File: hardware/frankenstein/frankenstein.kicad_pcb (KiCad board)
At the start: 2 copper layers, 100 x 99.9 mm, 261 parts, among them J351 MINI-USB-5P-3400020P1, M200 CONN_1, M201 CONN_1, M202 CONN_1, M351 CONN_1, M352 CONN_1, M401 CONN_1, M470 CONN_1, M471 CONN_1, P104 CONN_4, P201 CONN_10X2, P202 CONN_3, P203 CONN_2, P204 CONN_1, P205 CONN_1, P208 CONN_6, P209 CONN_6, P351 CONN_5X2, P352 MICRO-SDCARD-CONNECTOR-330006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, P353 CONN_10X2, P356 CONN_1, P401 CONN_3, P402 CONN_10X2, P403 CONN_16, P404 CONN_1, P405 CONN_1, P472 CONN_2, P51 CONN_4X2, P52 CONN_10X2, P53 CONN_2, P54 CONN_5X2, P55 CONN_6, P56 CONN_6, P57 CONN_6, P58 CONN_6, P603 CONN_6, P610 CONN_1, Q401 OVP_DRIVER, Q402 OVP_DRIVER, Q403 OVP_DRIVER, Q404 OVP_DRIVER, Q405 OVP_DRIVER, Q406 OVP_DRIVER, Q407 OVP_DRIVER, Q408 OVP_DRIVER, Q409 OVP_DRIVER, Q410 OVP_DRIVER, Q411 OVP_DRIVER, Q412 OVP_DRIVER, U101 MAX9926/9927, U201 LMV324IDR, U202 LMV324IDR, U203 LMV324IDR, U351 FT232RL, U471 SN65HVD230, U601 TC4427AVOA, U602 TC4427AVOA, U603 TC4427AVOA

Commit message: RC2
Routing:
- net GND: track 636.1 -> 611.2 mm, vias 267 -> 264
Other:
- net class Default: clearance 0.2032 -> 0.1778
- rule trace_clearance: 0.2032 -> 0.1778
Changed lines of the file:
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@@
   (general
     (links 592)
-    (no_connects 1)
+    (no_connects 0)
     (area 96.266 79.121 266.827001 205.740001)
     (thickness 1.6)
     (drawings 371)
-    (tracks 3153)
+    (tracks 3134)
     (zones 0)
     (modules 261)
@@
     (19 F.Paste user)
     (20 B.SilkS user)
-    (21 F.SilkS user)
+    (21 F.SilkS user hide)
     (22 B.Mask user)
     (23 F.Mask user)
@@
   (setup
     (last_trace_width 0.254)
-    (trace_clearance 0.2032)
+    (trace_clearance 0.1778)
     (zone_clearance 0.254)
     (zone_45_only no)
@@
     (pad_to_mask_clearance 0)
     (aux_axis_origin 0 0)
-    (visible_elements 7FFFFFBF)
+    (visible_elements 7FFFFFAF)
     (pcbplotparams
       (layerselection 318537729)
@@
   (net 185 GND)
   (net_class Default "This is the default net class."
-    (clearance 0.2032)
+    (clearance 0.1778)
     (trace_width 0.254)
     (via_dia 0.889)
@@
   (segment (start 164.465 126.365) (end 163.195 126.365) (width 0.254) (layer F.Cu) (net 70))
   (segment (start 127 149.819) (end 127 149.8194) (width 0.254) (layer F.Cu) (net 70))
+  (segment (start 127 142.19936) (end 126.95936 142.19936) (width 0.254) (layer F.Cu) (net 71))
+  (segment (start 121.919798 118.427702) (end 123.5075 116.84) (width 0.254) (layer F.Cu) (net 71))
+  (segment (start 121.919798 137.159798) (end 121.919798 118.427702) (width 0.254) (layer F.Cu) (net 71))
+  (segment (start 126.95936 142.19936) (end 121.919798 137.159798) (width 0.254) (layer F.Cu) (net 71))
   (segment (start 123.508 114.3) (end 123.508 115.57) (width 0.254) (layer F.Cu) (net 71))
   (segment (start 123.508 116.84) (end 123.5075 116.84) (width 0.254) (layer F.Cu) (net 71))
@@
   (segment (start 123.5075 115.5695) (end 123.5075 114.3) (width 0.254) (layer F.Cu) (net 71))
   (segment (start 123.508 115.57) (end 123.5075 115.5695) (width 0.254) (layer F.Cu) (net 71))
-  (segment (start 127 142.199) (end 127 142.1994) (width 0.254) (layer F.Cu) (net 71))
-  (segment (start 121.92 137.119) (end 127 142.199) (width 0.254) (layer F.Cu) (net 71))
-  (segment (start 121.92 118.11) (end 121.92 137.119) (width 0.254) (layer F.Cu) (net 71))
-  (segment (start 123.19 116.84) (end 121.92 118.11) (width 0.254) (layer F.Cu) (net 71))
-  (segment (start 123.5075 116.84) (end 123.19 116.84) (width 0.254) (layer F.Cu) (net 71))
   (segment (start 139.382 116.84) (end 139.382 115.57) (width 0.254) (layer F.Cu) (net 72))
   (segment (start 139.3825 116.84) (end 139.382 116.84) (width 0.254) (layer F.Cu) (net 72))
@@
   (segment (start 209.804 159.385) (end 210.439 160.02) (width 0.254) (layer F.Cu) (net 137))
   (segment (start 204.1525 159.385) (end 209.804 159.385) (width 0.254) (layer F.Cu) (net 137))
-  (segment (start 204.152 156.845) (end 204.1525 156.845) (width 0.254) (layer F.Cu) (net 138))
-  (segment (start 209.22 157.429) (end 210.439 156.21) (width 0.254) (layer F.Cu) (net 138))
-  (segment (start 205.105 157.429) (end 209.22 157.429) (width 0.254) (layer F.Cu) (net 138))
-  (segment (start 204.521 156.845) (end 205.105 157.429) (width 0.254) (layer F.Cu) (net 138))
-  (segment (start 204.1525 156.845) (end 204.521 156.845) (width 0.254) (layer F.Cu) (net 138))
+  (segment (start 204.1525 156.845) (end 204.597402 156.845) (width 0.254) (layer F.Cu) (net 138))
+  (segment (start 209.194802 157.454198) (end 210.439 156.21) (width 0.254) (layer F.Cu) (net 138))
+  (segment (start 205.2066 157.454198) (end 209.194802 157.454198) (width 0.254) (layer F.Cu) (net 138))
+  (segment (start 204.597402 156.845) (end 205.2066 157.454198) (width 0.254) (layer F.Cu) (net 138))
   (segment (start 164.38 186.826) (end 164.38 186.8255) (width 0.254) (layer F.Cu) (net 139))
   (segment (start 164.38 186.8255) (end 164.38 185.302) (width 0.254) (layer F.Cu) (net 139))
@@
   (segment (start 134.239 114.3) (end 137.4775 114.3) (width 0.254) (layer F.Cu) (net 184))
   (segment (start 137.4775 114.3) (end 137.478 114.3) (width 0.254) (layer F.Cu) (net 184))
+  (segment (start 198.438 174.7345) (end 196.7055 174.7345) (width 0.254) (layer F.Cu) (net 185))
+  (via (at 196.596 174.625) (size 0.889) (layers F.Cu B.Cu) (net 185))
+  (segment (start 196.7055 174.7345) (end 196.596 174.625) (width 0.254) (layer F.Cu) (net 185))
   (via (at 159.205 176.126) (size 0.889) (layers F.Cu B.Cu) (net 185))
   (via (at 156.03 176.126) (size 0.889) (layers F.Cu B.Cu) (net 185))
@@
   (via (at 151.448 119.062) (size 0.889) (layers F.Cu B.Cu) (net 185))
   (via (at 172.402 119.062) (size 0.889) (layers F.Cu B.Cu) (net 185))
-  (via (at 189.674 172.956) (size 0.889) (layers F.Cu B.Cu) (net 185))
   (via (at 183.896 189.53) (size 0.889) (layers F.Cu B.Cu) (net 185))
   (via (at 197.104 189.53) (size 0.889) (layers F.Cu B.Cu) (net 185))
@@
   (via (at 195.834 186.228) (size 0.889) (layers F.Cu B.Cu) (net 185))
   (via (at 199.136 184.704) (size 0.889) (layers F.Cu B.Cu) (net 185))
-  (via (at 184.15 166.797) (size 0.889) (layers F.Cu B.Cu) (net 185))
-  (via (at 184.023 168.702) (size 0.889) (layers F.Cu B.Cu) (net 185))
-  (via (at 193.421 172.956) (size 0.889) (layers F.Cu B.Cu) (net 185))
   (via (at 204.343 175.306) (size 0.889) (layers F.Cu B.Cu) (net 185))
   (via (at 209.55 175.306) (size 0.889) (layers F.Cu B.Cu) (net 185))
@@
   (segment (start 200.787 184.704) (end 200.914 184.577) (width 0.254) (layer F.Cu) (net 185))
   (segment (start 199.136 184.704) (end 200.787 184.704) (width 0.254) (layer F.Cu) (net 185))
-  (segment (start 188.087 166.67) (end 190.627 167.432) (width 0.254) (layer F.Cu) (net 185))
-  (segment (start 184.277 166.67) (end 188.087 166.67) (width 0.254) (layer F.Cu) (net 185))
-  (segment (start 184.15 166.797) (end 184.277 166.67) (width 0.254) (layer F.Cu) (net 185))
-  (segment (start 184.15 168.575) (end 184.15 166.797) (width 0.254) (layer B.Cu) (net 185))
-  (segment (start 184.023 168.702) (end 184.15 168.575) (width 0.254) (layer B.Cu) (net 185))
-  (segment (start 184.531 169.21) (end 184.023 168.702) (width 0.254) (layer F.Cu) (net 185))
-  (segment (start 184.531 170.988) (end 184.531 169.21) (width 0.254) (layer F.Cu) (net 185))
-  (segment (start 185.801 172.258) (end 184.531 170.988) (width 0.254) (layer F.Cu) (net 185))
-  (segment (start 188.976 172.258) (end 185.801 172.258) (width 0.254) (layer F.Cu) (net 185))
-  (segment (start 189.674 172.956) (end 188.976 172.258) (width 0.254) (layer F.Cu) (net 185))
-  (segment (start 189.674 172.956) (end 193.421 172.956) (width 0.254) (layer B.Cu) (net 185))
-  (segment (start 196.947 174.734) (end 198.438 174.734) (width 0.254) (layer F.Cu) (net 185))
-  (segment (start 196.629 175.052) (end 196.947 174.734) (width 0.254) (layer F.Cu) (net 185))
-  (segment (start 195.105 173.528) (end 196.629 175.052) (width 0.254) (layer F.Cu) (net 185))
-  (segment (start 193.992 173.528) (end 195.105 173.528) (width 0.254) (layer F.Cu) (net 185))
-  (segment (start 193.421 172.956) (end 193.992 173.528) (width 0.254) (layer F.Cu) (net 185))
   (segment (start 204.343 175.306) (end 209.55 175.306) (width 0.254) (layer B.Cu) (net 185))
   (segment (start 204.343 174.29) (end 204.343 175.306) (width 0.254) (layer F.Cu) (net 185))

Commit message: RC2
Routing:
- net /3.3V: track 215.7 -> 192.5 mm, vias 1 -> 2
- net GND: track 611.2 -> 607.9 mm

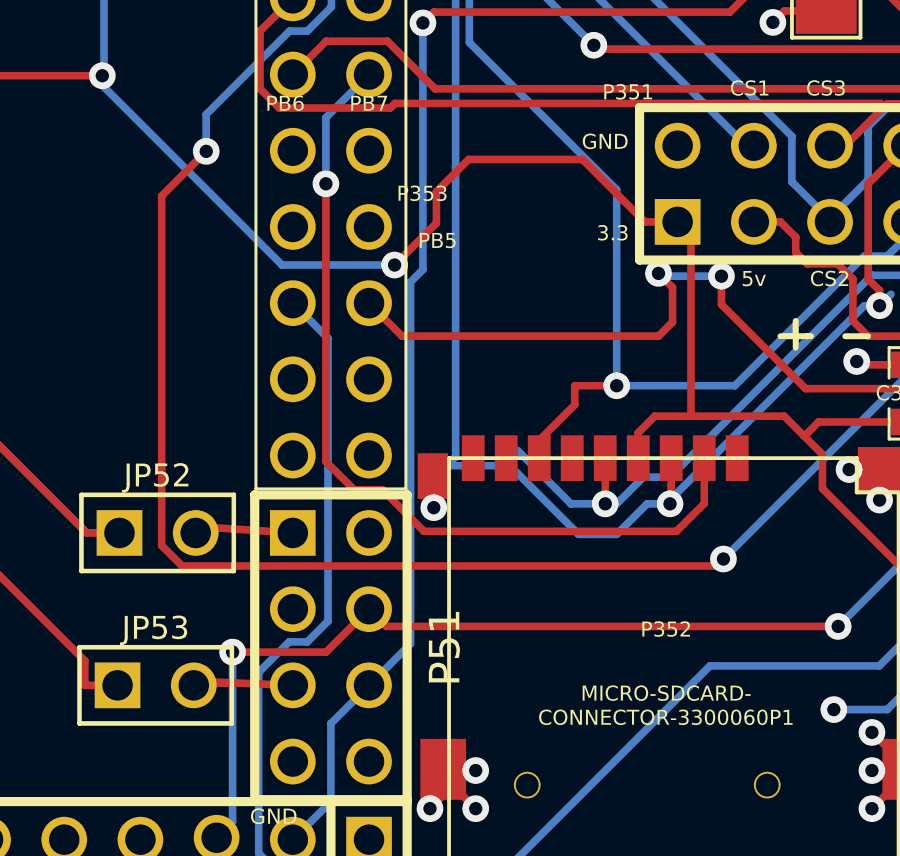
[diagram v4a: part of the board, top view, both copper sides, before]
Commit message: RX/TX flip
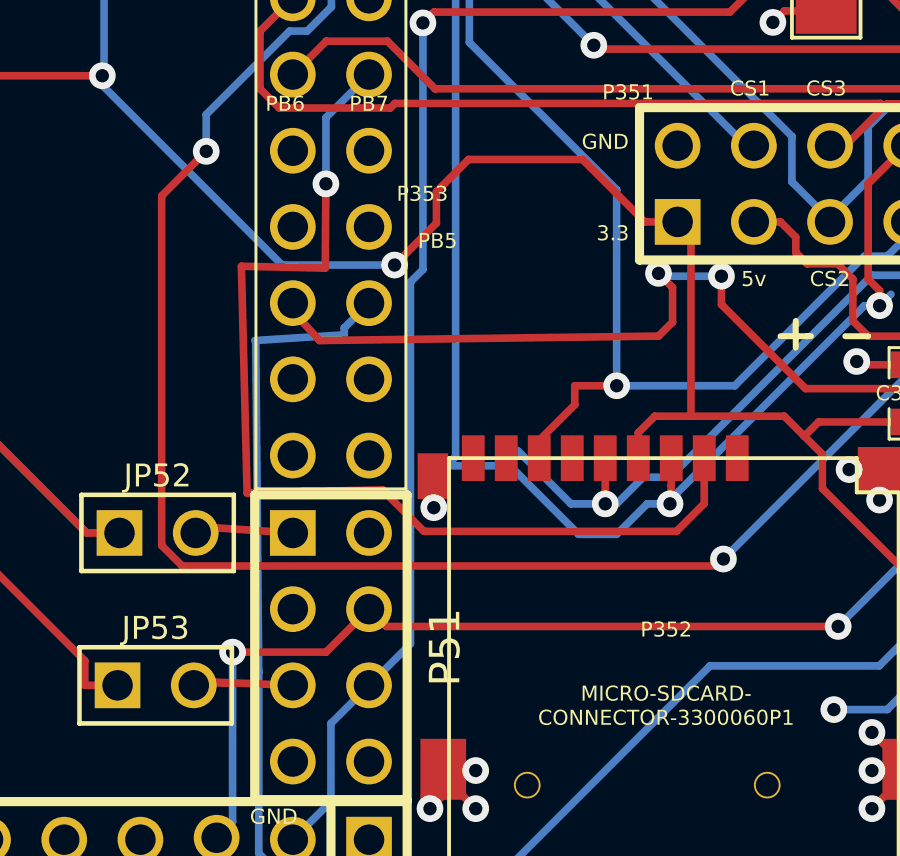
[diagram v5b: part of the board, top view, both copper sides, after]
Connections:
- P353 pad 15: /USART_TX -> /USART_RX
- P353 pad 16: /USART_RX -> /USART_TX
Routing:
- net /CS_SD_MODULE: track 29.0 -> 35.1 mm
- net /USART_RX: track 34.4 -> 37.1 mm
- net /USART_TX: track 88.1 -> 89.4 mm
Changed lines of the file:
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@@
     (thickness 1.6)
     (drawings 371)
-    (tracks 3119)
+    (tracks 3120)
     (zones 0)
     (modules 261)
@@
     (pad_to_mask_clearance 0)
     (aux_axis_origin 0 0)
-    (visible_elements 7FFFFF3F)
+    (visible_elements 7FFF9F3F)
     (pcbplotparams
       (layerselection 318537729)
@@
     (pad 15 thru_hole circle (at 6.30936 1.27 270) (size 1.524 1.524) (drill 1.016)
       (layers *.Cu *.Mask F.SilkS)
-      (net 103 /USART_TX)
+      (net 102 /USART_RX)
     )
     (pad 16 thru_hole circle (at 6.30936 -1.27 270) (size 1.524 1.524) (drill 1.016)
       (layers *.Cu *.Mask F.SilkS)
-      (net 102 /USART_RX)
+      (net 103 /USART_TX)
     )
     (pad 17 thru_hole circle (at 8.84936 1.27 270) (size 1.524 1.524) (drill 1.016)
@@
   (segment (start 200.787 167.432) (end 202.8817 169.5267) (width 0.254) (layer F.Cu) (net 16))
   (via (at 178.9026 168.702) (size 0.889) (layers F.Cu B.Cu) (net 17))
-  (segment (start 178.9026 177.9601) (end 178.9026 168.702) (width 0.254) (layer F.Cu) (net 17))
-  (segment (start 179.8451 178.9026) (end 178.9026 177.9601) (width 0.254) (layer F.Cu) (net 17))
-  (segment (start 180.7877 178.9026) (end 179.8451 178.9026) (width 0.254) (layer F.Cu) (net 17))
+  (segment (start 176.0855 171.45) (end 178.8795 171.5135) (width 0.254) (layer F.Cu) (net 17))
+  (segment (start 178.8795 171.5135) (end 178.9026 168.702) (width 0.254) (layer F.Cu) (net 17))
+  (segment (start 176.276 179.0065) (end 176.0855 171.45) (width 0.254) (layer F.Cu) (net 17))
+  (segment (start 180.7877 178.9026) (end 176.276 179.0065) (width 0.254) (layer F.Cu) (net 17))
   (segment (start 182.171 180.2859) (end 180.7877 178.9026) (width 0.254) (layer F.Cu) (net 17))
   (segment (start 190.5881 180.2859) (end 182.171 180.2859) (width 0.254) (layer F.Cu) (net 17))
@@
   (segment (start 190.0821 171.7815) (end 189.9884 171.6878) (width 0.254) (layer B.Cu) (net 102))
   (segment (start 192.0878 171.7815) (end 190.0821 171.7815) (width 0.254) (layer B.Cu) (net 102))
-  (segment (start 181.4386 173.778) (end 180.34 172.6794) (width 0.254) (layer F.Cu) (net 102))
-  (segment (start 189.9923 173.778) (end 181.4386 173.778) (width 0.254) (layer F.Cu) (net 102))
+  (segment (start 178.689 173.9265) (end 177.673 172.8064) (width 0.254) (layer F.Cu) (net 102))
+  (segment (start 189.9923 173.778) (end 178.689 173.9265) (width 0.254) (layer F.Cu) (net 102))
   (segment (start 190.4579 173.3124) (end 189.9923 173.778) (width 0.254) (layer F.Cu) (net 102))
   (segment (start 190.4579 172.1573) (end 190.4579 173.3124) (width 0.254) (layer F.Cu) (net 102))
   (segment (start 189.9884 171.6878) (end 190.4579 172.1573) (width 0.254) (layer F.Cu) (net 102))
+  (segment (start 179.5145 173.736) (end 179.5145 173.50486) (width 0.254) (layer B.Cu) (net 103))
+  (segment (start 176.53 173.9265) (end 179.5145 173.736) (width 0.254) (layer B.Cu) (net 103))
+  (segment (start 179.5145 173.50486) (end 180.34 172.67936) (width 0.254) (layer B.Cu) (net 103))
   (via (at 214.44 178.735) (size 0.889) (layers F.Cu B.Cu) (net 103))
   (segment (start 216.027 178.164) (end 216.154 178.036) (width 0.254) (layer F.Cu) (net 103))
@@
   (segment (start 215.9 174.163) (end 215.773 172.893) (width 0.254) (layer F.Cu) (net 103))
   (segment (start 216.154 178.036) (end 215.9 174.163) (width 0.254) (layer F.Cu) (net 103))
-  (segment (start 176.6638 184.9824) (end 177.6736 183.9726) (width 0.254) (layer B.Cu) (net 103))
+  (segment (start 176.6638 184.9824) (end 176.657 184.2135) (width 0.254) (layer B.Cu) (net 103))
   (via (at 215.773 169.718) (size 0.889) (layers F.Cu B.Cu) (net 103))
   (via (at 210.058 168.194) (size 0.889) (layers F.Cu B.Cu) (net 103))
@@
   (segment (start 207.2678 168.622) (end 206.8398 169.05) (width 0.254) (layer F.Cu) (net 103))
   (segment (start 207.268 168.622) (end 207.2678 168.622) (width 0.254) (layer F.Cu) (net 103))
-  (segment (start 178.9718 173.8512) (end 177.8 172.6794) (width 0.254) (layer B.Cu) (net 103))
-  (segment (start 178.9718 183.2854) (end 178.9718 173.8512) (width 0.254) (layer B.Cu) (net 103))
-  (segment (start 178.2846 183.9726) (end 178.9718 183.2854) (width 0.254) (layer B.Cu) (net 103))
-  (segment (start 177.6736 183.9726) (end 178.2846 183.9726) (width 0.254) (layer B.Cu) (net 103))
+  (segment (start 176.657 184.2135) (end 176.5647 173.9383) (width 0.254) (layer B.Cu) (net 103))
   (via (at 187.833 164.084) (size 0.889) (layers F.Cu B.Cu) (net 104))
   (via (at 185.547 161.798) (size 0.889) (layers F.Cu B.Cu) (net 104))

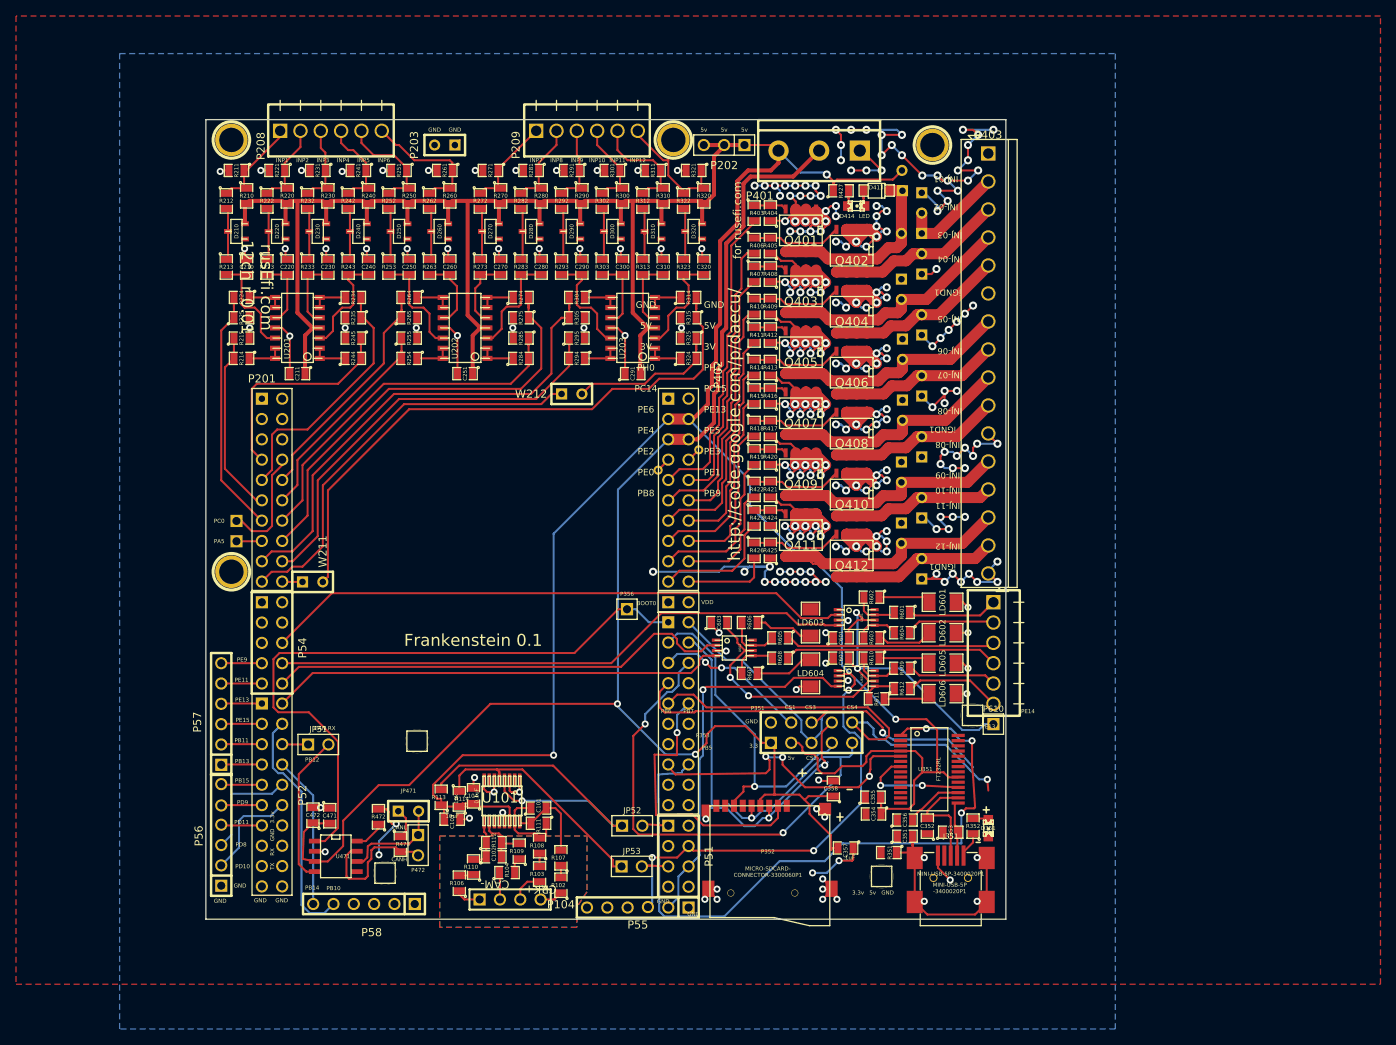
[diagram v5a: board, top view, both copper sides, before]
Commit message: 
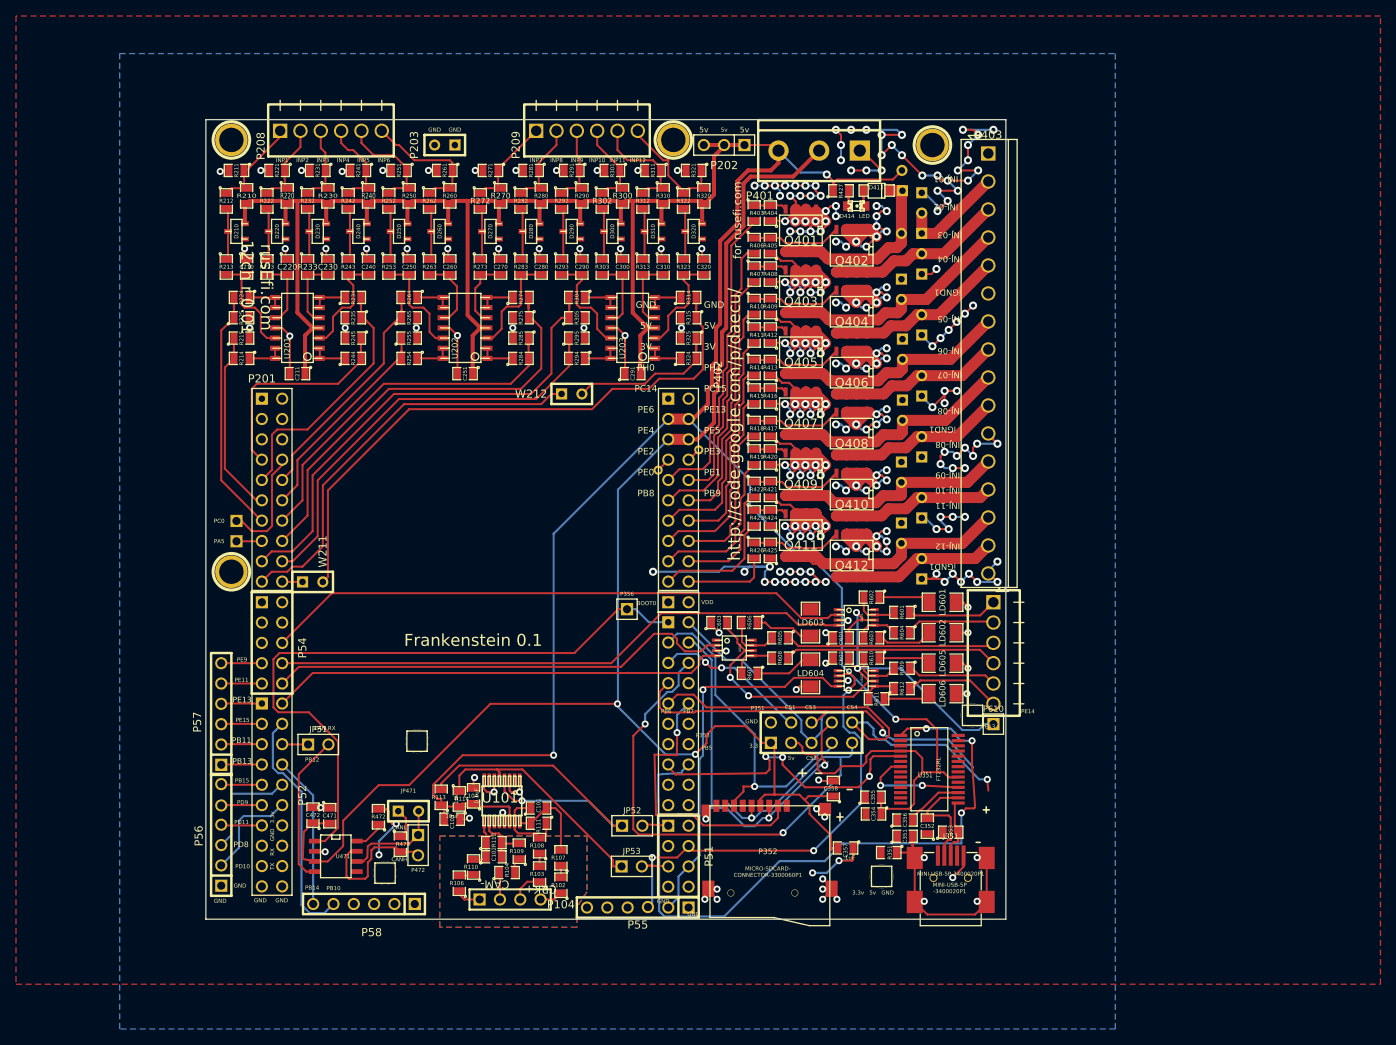
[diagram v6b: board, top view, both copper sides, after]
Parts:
- removed D351: GREEN, LED-0805
- removed R352: 1k, SM0805
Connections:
- J351 pad 1: F-0000107 -> GND
- J351 pad 2: F-0000108 -> (no net)
- J351 pad 3: F-0000115 -> F-0000108
- J351 pad 4: (no net) -> F-0000115
- J351 pad 5: GND -> F-0000107
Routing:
- net F-0000107: track 3.23 -> 0.00 mm
- net F-0000109: track 1.97 -> 0.00 mm
- net F-0000108: track 8.93 -> 10.4 mm
- net F-0000115: track 13.8 -> 14.4 mm
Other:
- board text added: "IN10"
- board text added: "IN11"
